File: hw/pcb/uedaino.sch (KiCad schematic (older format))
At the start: 6 parts, among them IC1 ATMEGA328P-A, SW1 SW_PUSH

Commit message: Add functions
Add power circuit.
Add Capacitive Touch Sensor circuit.
Add pin header.
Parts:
- added C4, C5: 10uF, Capacitors_SMD:C_0603_HandSoldering, symbol C_Small
- added C6, C7: 22uF, Capacitors_SMD:C_0603_HandSoldering, symbol C_Small
- added D1: LED_+5V, Diodes_SMD:D_0603, symbol Led_Small
- added D2: LED_+3V3, Diodes_SMD:D_0603, symbol Led_Small
- added JP1, JP2, JP3, JP4, JP5, JP6, JP7, JP8, JP9: Jumper_NC_Small, Pin_Headers:Pin_Header_Straight_1x02, symbol Jumper_NC_Small
- added P1: CN_PWR, Connect:BARREL_JACK, symbol CONN_01X02
- added P2: CN_UART, Pin_Headers:Pin_Header_Straight_1x05, symbol CONN_01X05
- added P3: CN_HEADER1, Pin_Headers:Pin_Header_Straight_1x15, symbol CONN_01X15
- added P4: CN_I2C, Pin_Headers:Pin_Header_Straight_1x04, symbol CONN_01X04
- added P5: CN_HEADER2, Pin_Headers:Pin_Header_Straight_1x15, symbol CONN_01X15
- added P6: CN_ICSP, Pin_Headers:Pin_Header_Straight_2x03, symbol CONN_02X03
- added R2: 10M, Resistors_SMD:R_0603_HandSoldering, symbol R_Small
- added R3, R4: 1K, Resistors_SMD:R_0603_HandSoldering, symbol R_Small
- added R5, R6: 4.7K, Resistors_SMD:R_0603_HandSoldering, symbol R_Small
- added SW2: SW_PWSEL, Pin_Headers:Pin_Header_Straight_1x03, symbol SWITCH_INV
- added U1: AP1117, TO_SOT_Packages_SMD:SOT-223, symbol AP1117
- added Y1: 16MHz, Crystals:Crystal_HC49-SD_SMD, symbol Crystal_Small
- C1, C2, C3: footprint Capacitors_SMD:C_0603 -> Capacitors_SMD:C_0603_HandSoldering
- R1: footprint Resistors_SMD:R_0603 -> Resistors_SMD:R_0603_HandSoldering
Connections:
- net labels added: +3.3V, A0, A1, A2, A3, A4/SDA, A5/SCL, A6, A7, D10, D11, D12, D13, D2, D3, D4, D5, D6, D7, D8, D9, PWR_USB, XT1, XT2
- net labels removed: +5C
- wire segments 24 -> 156
- no-connect marks 0 -> 2
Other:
- note added: "AP1117 Compatible parts\nAkizuki LT1117CST-3.3\nAitendo AMS1117"
- note added: "Akizuki 16MHZ P-01767\nHC-49/S"
- note added: "CAPACITIVE SENSOR"
- note added: "I2C"
- note added: "ICSP"
- note added: "POWER"
- note added: "PWR_LED"
- note added: "UART"
- note added: "XTAL"
- note added: "aitendo AKIT-DTR340MC"
- moved on the sheet: C1, C2, C3, IC1, R1, SW1

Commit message: Support Arduino Pinout
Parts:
- removed P3: CN_HEADER1, Pin_Headers:Pin_Header_Straight_1x15, symbol CONN_01X15
- removed P5: CN_HEADER2, Pin_Headers:Pin_Header_Straight_1x15, symbol CONN_01X15
- added P3: ANALOG_IN, Socket_Strips:Socket_Strip_Straight_1x06, symbol CONN_01X06
- added P5: POWER, Socket_Strips:Socket_Strip_Straight_1x08, symbol CONN_01X08
- added P7: DIGITAL, Socket_Strips:Socket_Strip_Straight_1x18, symbol CONN_01X18
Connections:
- net labels added: AREF
- net labels removed: A6, A7
- wire segments 156 -> 154
- no-connect marks 2 -> 4

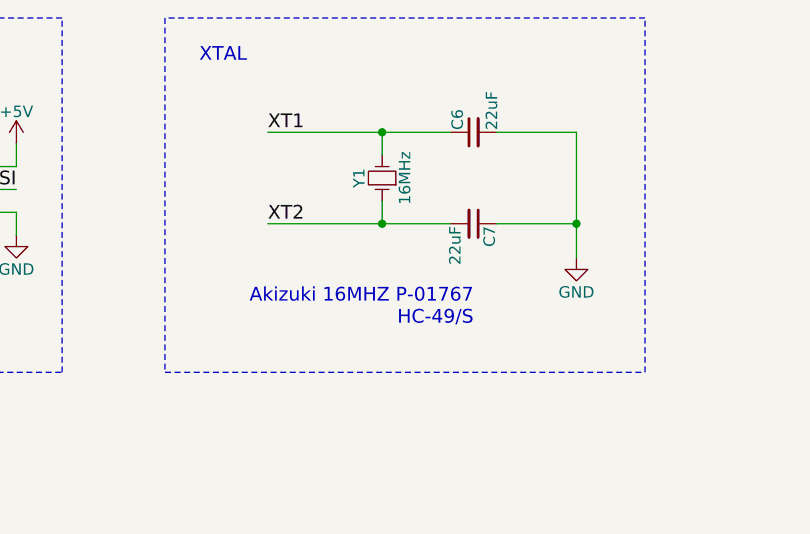
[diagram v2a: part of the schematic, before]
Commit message: Remove XTAL
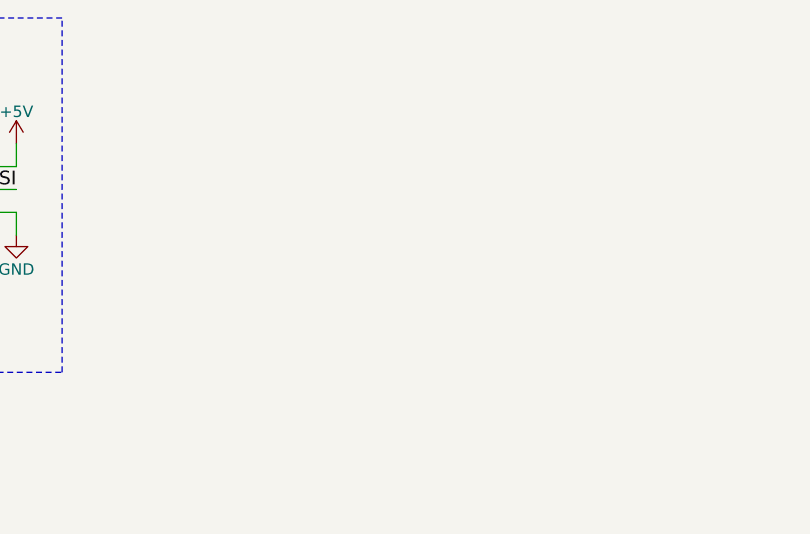
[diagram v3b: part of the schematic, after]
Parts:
- removed C6, C7: 22uF, Capacitors_SMD:C_0603_HandSoldering, symbol C_Small
- removed Y1: 16MHz, Crystals:Crystal_HC49-SD_SMD, symbol Crystal_Small
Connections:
- wire segments 154 -> 147
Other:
- note removed: "Akizuki 16MHZ P-01767\nHC-49/S"
- note removed: "XTAL"
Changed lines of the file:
@@
 	1    0    0    -1
 $EndComp
-$Comp
-L Crystal_Small Y1
-U 1 1 585D59B5
-P 8050 1250
-F 0 "Y1" H 8050 1350 50  0000 C CNN
-F 1 "16MHz" H 8050 1150 50  0000 C CNN
-F 2 "Crystals:Crystal_HC49-SD_SMD" H 8050 1250 50  0001 C CNN
-F 3 "" H 8050 1250 50  0000 C CNN
-	1    8050 1250
-	0    -1   -1   0
-$EndComp
-Text Label 7550 1050 0    60   ~ 0
-XT1
-Text Label 7550 1450 0    60   ~ 0
-XT2
-$Comp
-L C_Small C6
-U 1 1 585D5BAA
-P 8450 1050
-F 0 "C6" H 8460 1120 50  0000 L CNN
-F 1 "22uF" H 8460 970 50  0000 L CNN
-F 2 "Capacitors_SMD:C_0603_HandSoldering" H 8450 1050 50  0001 C CNN
-F 3 "" H 8450 1050 50  0000 C CNN
-	1    8450 1050
-	0    -1   -1   0
-$EndComp
-$Comp
-L C_Small C7
-U 1 1 585D5BEB
-P 8450 1450
-F 0 "C7" H 8460 1520 50  0000 L CNN
-F 1 "22uF" H 8460 1370 50  0000 L CNN
-F 2 "Capacitors_SMD:C_0603_HandSoldering" H 8450 1450 50  0001 C CNN
-F 3 "" H 8450 1450 50  0000 C CNN
-	1    8450 1450
-	0    1    1    0
-$EndComp
-$Comp
-L GND #PWR018
-U 1 1 585D5DF9
-P 8900 1600
-F 0 "#PWR018" H 8900 1350 50  0001 C CNN
-F 1 "GND" H 8900 1450 50  0000 C CNN
-F 2 "" H 8900 1600 50  0000 C CNN
-F 3 "" H 8900 1600 50  0000 C CNN
-	1    8900 1600
-	1    0    0    -1
-$EndComp
-Text Notes 7250 750  0    60   ~ 0
-XTAL
 Text Notes 900  4000 0    60   ~ 0
 CAPACITIVE SENSOR
@@
 Text Label 8800 4900 2    60   ~ 0
 TXD
-Text Notes 8450 1900 2    60   ~ 0
-Akizuki 16MHZ P-01767\nHC-49/S
 $Comp
 L CONN_01X06 P3
@@
 	6650 550  5150 550
 Wire Wire Line
-	8050 1350 8050 1450
-Wire Wire Line
-	7550 1450 8350 1450
-Wire Wire Line
-	8050 1150 8050 1050
-Wire Wire Line
-	7550 1050 8350 1050
-Connection ~ 8050 1450
-Connection ~ 8050 1050
-Wire Wire Line
-	8550 1050 8900 1050
-Wire Wire Line
-	8900 1050 8900 1600
-Wire Wire Line
-	8550 1450 8900 1450
-Connection ~ 8900 1450
-Wire Notes Line
-	7100 550  7100 2100
-Wire Notes Line
-	7100 2100 9200 2100
-Wire Notes Line
-	9200 2100 9200 550
-Wire Notes Line
-	9200 550  7100 550
-Wire Wire Line
 	1300 4850 1300 5700

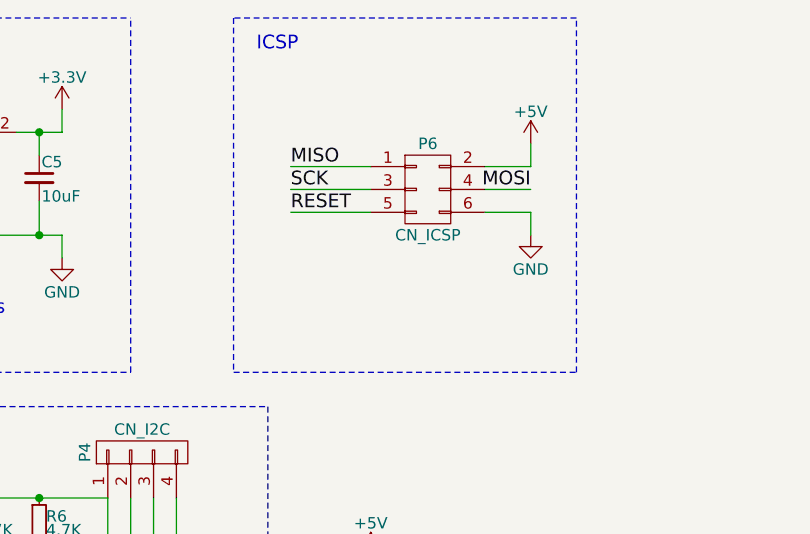
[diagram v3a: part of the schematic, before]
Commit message: Remove ICSP
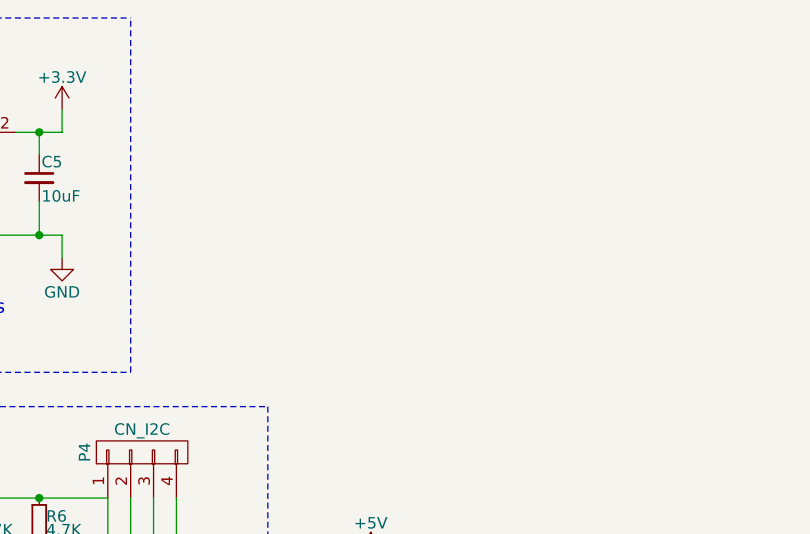
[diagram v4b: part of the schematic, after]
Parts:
- removed P6: CN_ICSP, Pin_Headers:Pin_Header_Straight_2x03, symbol CONN_02X03
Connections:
- wire segments 147 -> 139
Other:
- note removed: "ICSP"
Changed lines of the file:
@@
 PWR_LED
-$Comp
-L CONN_02X03 P6
-U 1 1 585CE266
-P 6000 1300
-F 0 "P6" H 6000 1500 50  0000 C CNN
-F 1 "CN_ICSP" H 6000 1100 50  0000 C CNN
-F 2 "Pin_Headers:Pin_Header_Straight_2x03" H 6000 100 50  0001 C CNN
-F 3 "" H 6000 100 50  0000 C CNN
-	1    6000 1300
-	1    0    0    -1
-$EndComp
-$Comp
-L GND #PWR015
-U 1 1 585CFA07
-P 6450 1500
-F 0 "#PWR015" H 6450 1250 50  0001 C CNN
-F 1 "GND" H 6450 1350 50  0000 C CNN
-F 2 "" H 6450 1500 50  0000 C CNN
-F 3 "" H 6450 1500 50  0000 C CNN
-	1    6450 1500
-	1    0    0    -1
-$EndComp
-$Comp
-L +5V #PWR016
-U 1 1 585CFA3D
-P 6450 1100
-F 0 "#PWR016" H 6450 950 50  0001 C CNN
-F 1 "+5V" H 6450 1240 50  0000 C CNN
-F 2 "" H 6450 1100 50  0000 C CNN
-F 3 "" H 6450 1100 50  0000 C CNN
-	1    6450 1100
-	1    0    0    -1
-$EndComp
-Text Label 6450 1300 2    60   ~ 0
-MOSI
-Text Label 5400 1200 0    60   ~ 0
-MISO
-Text Label 5400 1300 0    60   ~ 0
-SCK
-Text Label 5400 1400 0    60   ~ 0
-RESET
-Text Notes 5250 700  0    60   ~ 0
-ICSP
 $Comp
 L +5V #PWR017
@@
 	3500 2250 2500 2250
 Wire Wire Line
-	6250 1200 6450 1200
-Wire Wire Line
-	6450 1200 6450 1100
-Wire Wire Line
-	6250 1400 6450 1400
-Wire Wire Line
-	6450 1400 6450 1500
-Wire Wire Line
-	6450 1300 6250 1300
-Wire Wire Line
-	5750 1200 5400 1200
-Wire Wire Line
-	5750 1300 5400 1300
-Wire Wire Line
-	5750 1400 5400 1400
-Wire Notes Line
-	5150 550  5150 2100
-Wire Notes Line
-	5150 2100 6650 2100
-Wire Notes Line
-	6650 2100 6650 550
-Wire Notes Line
-	6650 550  5150 550
-Wire Wire Line
 	1300 4850 1300 5700

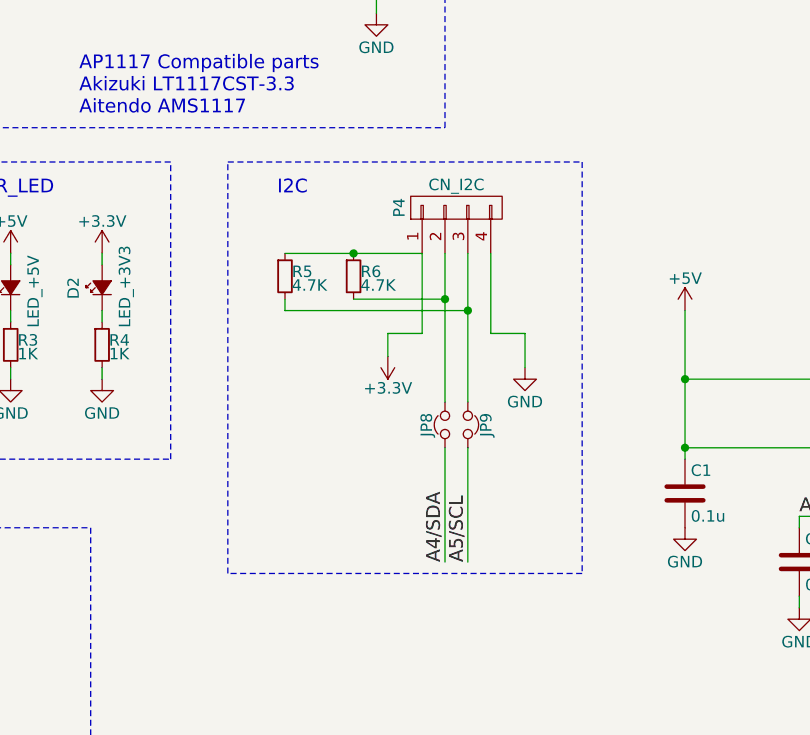
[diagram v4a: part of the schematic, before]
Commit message: Remove I2C
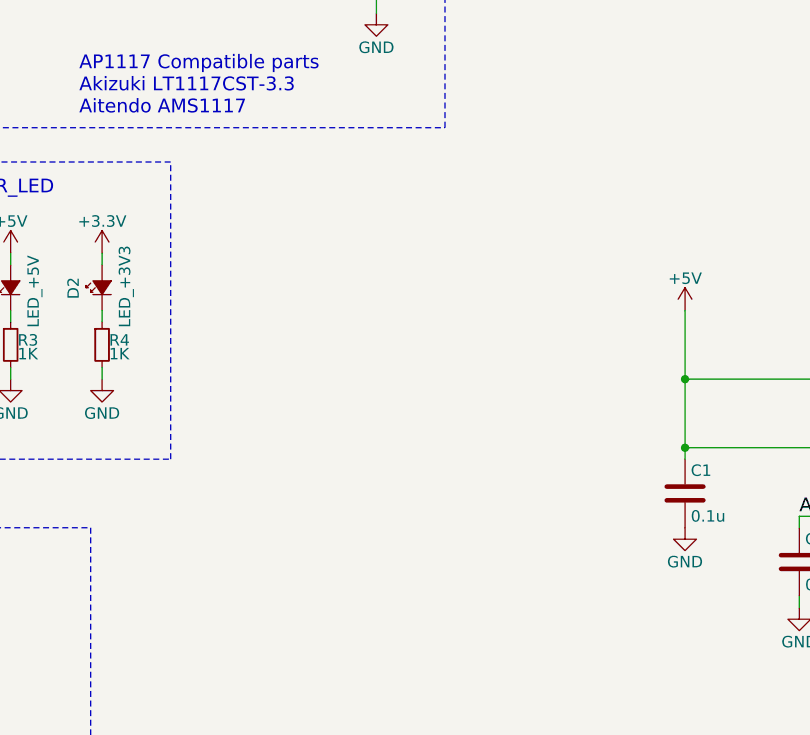
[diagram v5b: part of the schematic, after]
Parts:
- removed JP8, JP9: Jumper_NC_Small, Pin_Headers:Pin_Header_Straight_1x02, symbol Jumper_NC_Small
- removed P4: CN_I2C, Pin_Headers:Pin_Header_Straight_1x04, symbol CONN_01X04
- removed R5, R6: 4.7K, Resistors_SMD:R_0603_HandSoldering, symbol R_Small
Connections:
- wire segments 139 -> 125
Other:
- note removed: "I2C"
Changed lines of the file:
@@
 Text Label 9750 3700 2    60   ~ 0
 D13
-Text Notes 4100 2400 2    60   ~ 0
-I2C
-$Comp
-L CONN_01X04 P4
-U 1 1 585DE189
-P 4750 2450
-F 0 "P4" H 4750 2700 50  0000 C CNN
-F 1 "CN_I2C" V 4850 2450 50  0000 C CNN
-F 2 "Pin_Headers:Pin_Header_Straight_1x04" H 4750 2450 50  0001 C CNN
-F 3 "" H 4750 2450 50  0000 C CNN
-	1    4750 2450
-	0    -1   -1   0
-$EndComp
-$Comp
-L +3.3V #PWR019
-U 1 1 585DE564
-P 4450 3100
-F 0 "#PWR019" H 4450 2950 50  0001 C CNN
-F 1 "+3.3V" H 4450 3240 50  0000 C CNN
-F 2 "" H 4450 3100 50  0000 C CNN
-F 3 "" H 4450 3100 50  0000 C CNN
-	1    4450 3100
-	1    0    0    1
-$EndComp
-$Comp
-L GND #PWR020
-U 1 1 585DE5A6
-P 5050 3150
-F 0 "#PWR020" H 5050 2900 50  0001 C CNN
-F 1 "GND" H 5050 3000 50  0000 C CNN
-F 2 "" H 5050 3150 50  0000 C CNN
-F 3 "" H 5050 3150 50  0000 C CNN
-	1    5050 3150
-	1    0    0    -1
-$EndComp
-$Comp
-L Jumper_NC_Small JP9
-U 1 1 585DF97F
-P 4800 3400
-F 0 "JP9" H 4800 3480 50  0000 C CNN
-F 1 "Jumper_NC_Small" H 4810 3340 50  0001 C CNN
-F 2 "Pin_Headers:Pin_Header_Straight_1x02" H 4800 3400 50  0001 C CNN
-F 3 "" H 4800 3400 50  0000 C CNN
-	1    4800 3400
-	0    1    1    0
-$EndComp
-$Comp
-L Jumper_NC_Small JP8
-U 1 1 585DF9CC
-P 4700 3400
-F 0 "JP8" H 4700 3480 50  0000 C CNN
-F 1 "Jumper_NC_Small" H 4710 3340 50  0001 C CNN
-F 2 "Pin_Headers:Pin_Header_Straight_1x02" H 4700 3400 50  0001 C CNN
-F 3 "" H 4700 3400 50  0000 C CNN
-	1    4700 3400
-	0    -1   -1   0
-$EndComp
-$Comp
-L R_Small R6
-U 1 1 585DFA80
-P 4300 2750
-F 0 "R6" H 4330 2770 50  0000 L CNN
-F 1 "4.7K" H 4330 2710 50  0000 L CNN
-F 2 "Resistors_SMD:R_0603_HandSoldering" H 4300 2750 50  0001 C CNN
-F 3 "" H 4300 2750 50  0000 C CNN
-	1    4300 2750
-	1    0    0    -1
-$EndComp
-$Comp
-L R_Small R5
-U 1 1 585DFAD3
-P 4000 2750
-F 0 "R5" H 4030 2770 50  0000 L CNN
-F 1 "4.7K" H 4030 2710 50  0000 L CNN
-F 2 "Resistors_SMD:R_0603_HandSoldering" H 4000 2750 50  0001 C CNN
-F 3 "" H 4000 2750 50  0000 C CNN
-	1    4000 2750
-	1    0    0    -1
-$EndComp
-Text Label 4700 4000 1    60   ~ 0
-A4/SDA
-Text Label 4800 4000 1    60   ~ 0
-A5/SCL
 $Comp
 L Jumper_NC_Small JP1
@@
 Connection ~ 9350 3700
 Wire Wire Line
-	4600 2650 4600 3000
-Wire Wire Line
-	4600 3000 4450 3000
-Wire Wire Line
-	4450 3000 4450 3100
-Wire Wire Line
-	4900 2650 4900 3000
-Wire Wire Line
-	4900 3000 5050 3000
-Wire Wire Line
-	5050 3000 5050 3150
-Wire Wire Line
-	4700 2650 4700 3300
-Wire Wire Line
-	4800 2650 4800 3300
-Wire Wire Line
-	4000 2650 4600 2650
-Wire Wire Line
-	4300 2850 4700 2850
-Connection ~ 4700 2850
-Wire Wire Line
-	4000 2850 4000 2900
-Wire Wire Line
-	4000 2900 4800 2900
-Connection ~ 4800 2900
-Wire Wire Line
-	4800 3500 4800 4000
-Wire Wire Line
-	4700 3500 4700 4000
-Wire Notes Line
-	3750 2250 5300 2250
-Wire Notes Line
-	5300 2250 5300 4050
-Wire Notes Line
-	5300 4050 3750 4050
-Wire Notes Line
-	3750 4050 3750 2250
-Wire Wire Line
 	1300 4550 1300 4650
 Wire Wire Line
@@
 Wire Notes Line
 	3150 6300 800  6300
-Connection ~ 4300 2650
 Wire Wire Line
 	4500 6000 3850 6000
